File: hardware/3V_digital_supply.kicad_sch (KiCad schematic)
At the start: 0 parts

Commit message: Finalize power
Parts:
- added C601: 1.0uF, symbol Device:C
- added C602: 100pF, symbol Device:C_Small
- added C603: 2.2uF, symbol Device:C
- added U601: AP2210K-3.3, Package_TO_SOT_SMD:SOT-23-5, symbol carrier-wave:AP2210K-3.3TRG1
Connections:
- new net: C602.1, U601.4 (BYP)
- new net +3.3VD: C603.1, U601.5 (VOUT)
- new net GND: C601.2, C602.2, C603.2, U601.2 (GND)
- new net VBUS_F: C601.1, U601.1 (VIN), U601.3 (EN)
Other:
- note added: "Dropout @ 100mA: 300mV Dropout @ 300mA: 500mV"
- company: (none) -> Jacob Wigent
- title: (none) -> 3.3V Digital Regulator

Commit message: Cleanup Sheets
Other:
- note added: "5V USB input is regulated to 3.3V for digital components using LDO. Input and output capacitors follow datasheet recomendations."
- note added: "AP2210K-3.3"
- note added: "Description"

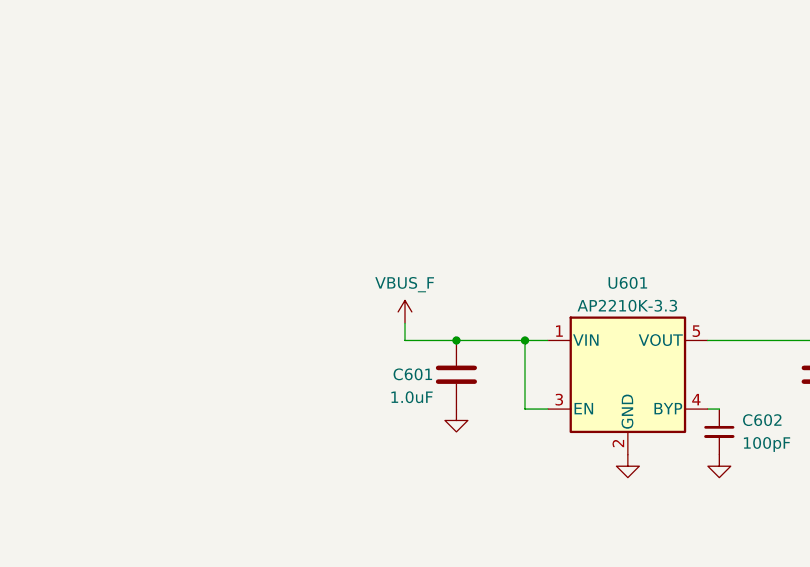
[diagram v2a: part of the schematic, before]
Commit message: Rename VBUS_F to VBUS
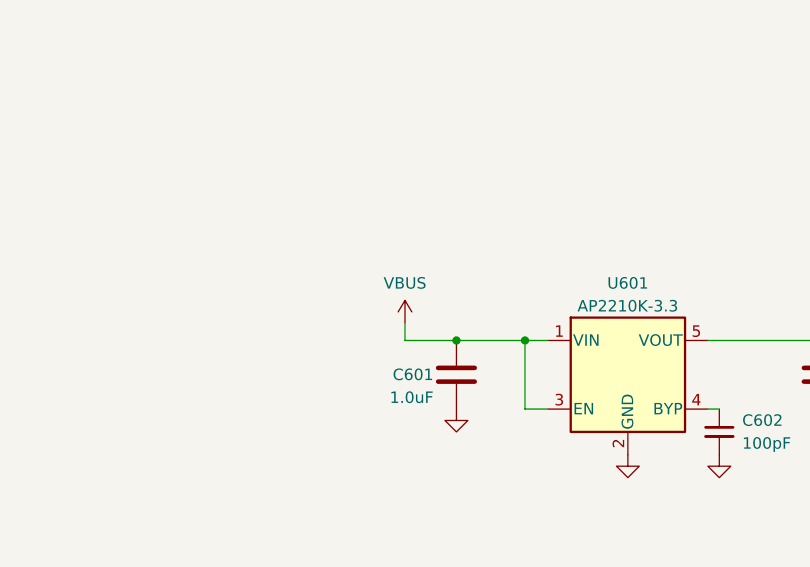
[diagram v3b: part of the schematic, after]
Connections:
- net VBUS_F renamed VBUS
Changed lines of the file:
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@@
 			)
 		)
-		(property "Value" "VBUS_F"
+		(property "Value" "VBUS"
 			(at 112.395 87.63 0)
 			(show_name no)
